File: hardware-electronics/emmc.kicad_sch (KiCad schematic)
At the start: 2 parts, among them U2 EMMC16G-MW28-01E10, U8 USB2244-AEZG-06

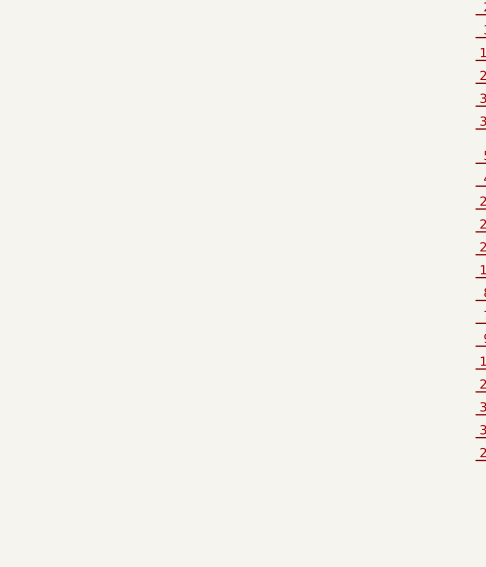
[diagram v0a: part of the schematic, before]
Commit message: SCH organise schematic #7
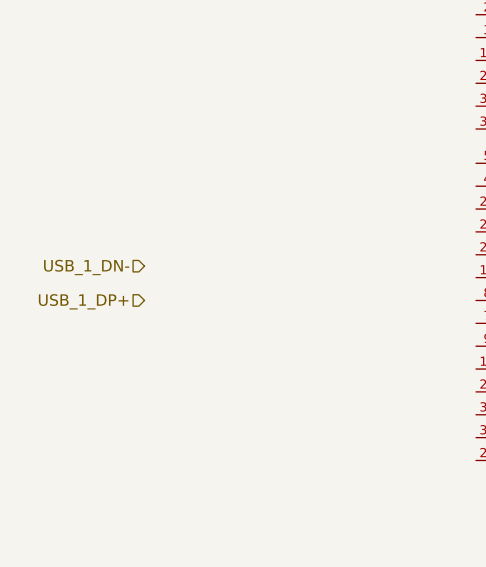
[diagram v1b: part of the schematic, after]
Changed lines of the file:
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@@
 	(generator_version "8.0")
 	(paper "A4")
+	(hierarchical_label "USB_1_DP+"
+		(shape input)
+		(at 58.42 54.61 180)
+		(fields_autoplaced yes)
+		(effects
+			(font
+				(size 1.27 1.27)
+			)
+			(justify right)
+		)
+	)
+	(hierarchical_label "USB_1_DN-"
+		(shape input)
+		(at 58.42 50.8 180)
+		(fields_autoplaced yes)
+		(effects
+			(font
+				(size 1.27 1.27)
+			)
+			(justify right)
+		)
+	)
 	(symbol
 		(lib_id "M2SmartHomeSymbols:USB2244-AEZG-06")

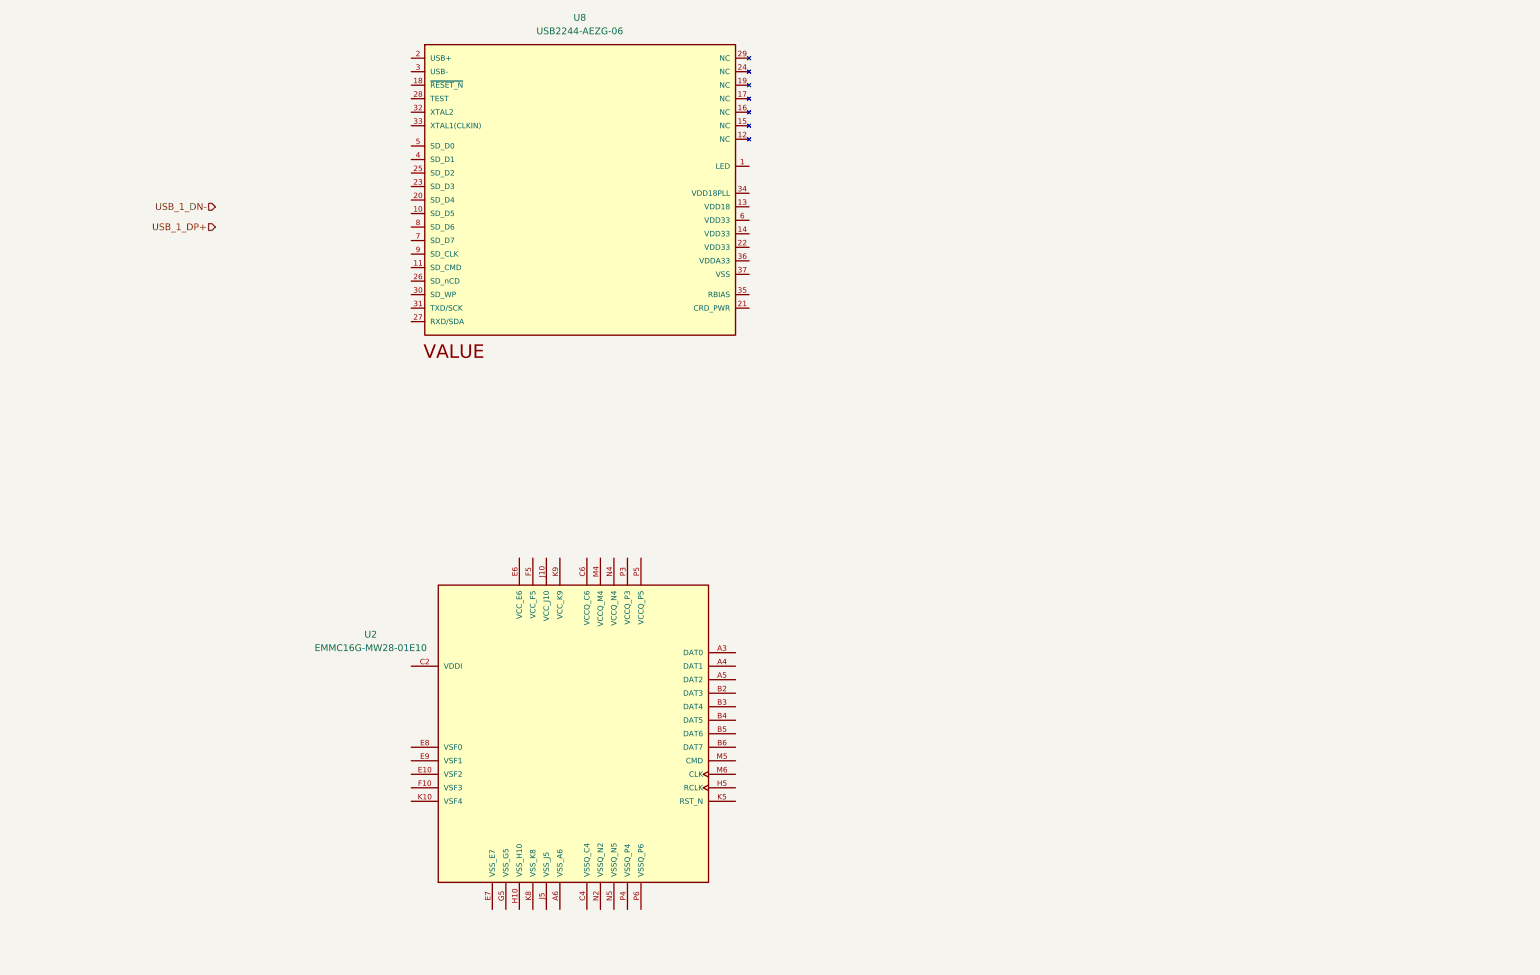
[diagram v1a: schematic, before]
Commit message: WIP SCH EMMC section
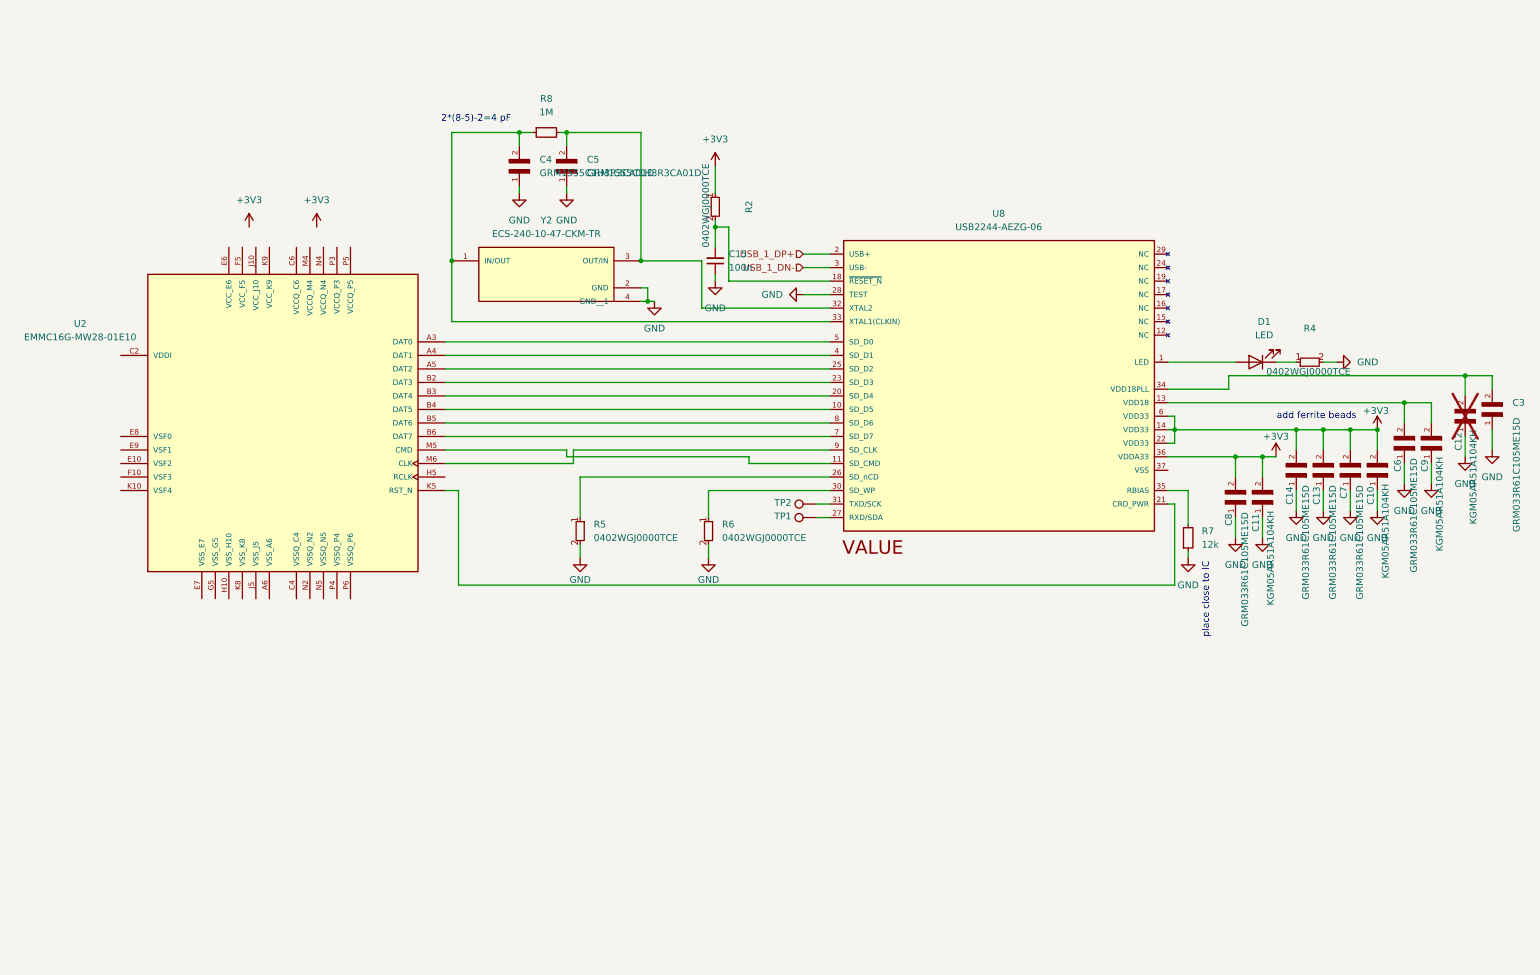
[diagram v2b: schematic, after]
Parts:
- added C10, C11, C12, C9: KGM05AR51A104KH, M2SmartHomeFootprints:KGM05AR51A104KH, symbol M2SmartHomeSymbols:KGM05AR51A104KH
- added C13, C14, C3, C6, C7, C8: GRM033R61C105ME15D, M2SmartHomeFootprints:GRM033R61C105ME15D, symbol M2SmartHomeSymbols:GRM033R61C105ME15D
- added C15: C_100n_0402, C_100n_0402:C_0402_1005Metric, symbol M2SmartHomeSymbols:C_100n_0402
- added C4, C5: GRM1555C1H3R3CA01D, GRM1555C1H3R3CA01D:CAPC1005X55N, symbol M2SmartHomeSymbols:GRM1555C1H3R3CA01D
- added D1: LED, M2SmartHomeFootprints:LED_KPT-1608ZGC, symbol M2SmartHomeSymbols:KP-1608CGCK
- added R2, R4, R5, R6: 0402WGJ0000TCE, M2SmartHomeFootprints:0402WGJ0000TCE, symbol M2SmartHomeSymbols:0402WGJ0000TCE
- added R7: R_12k_0402, R_12k_0402:R_0402_1005Metric, symbol M2SmartHomeSymbols:R_12k_0402
- added R8: R_1M_0402, R_1M_0402:R_0402_1005Metric, symbol M2SmartHomeSymbols:R_1M_0402
- added TP1: TestPoint, TestPoint:TestPoint_Pad_D1.0mm, symbol Connector:TestPoint
- added TP2: TestPoint, symbol Connector:TestPoint
- added Y2: ECS-240-10-47-CKM-TR, M2SmartHomeFootprints:ECS-240-10-47-CKM-TR, symbol M2SmartHomeSymbols:ECS-240-10-47-CKM-TR
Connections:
- net USB_1_DN-: now also U8.3 (USB-)
- net USB_1_DP+: now also U8.2 (USB+)
- net at U8.1 (LED): now also D1.2 (A)
- net at U8.10 (SD_D5): now also U2.B4 (DAT5)
- net at U8.11 (SD_CMD): now also U2.M5 (CMD)
- net at U8.13 (VDD18): now also C6.2, C9.2
- net +3V3: now reaches U8.14 (VDD33)
- net +3V3: now also U8.22 (VDD33), U8.36 (VDDA33), U8.6 (VDD33), C10.2, C11.2, C13.2, C14.2, C7.2, C8.2, R2.1
- net at U8.18 (~{RESET_N}): now also C15.2, R2.2
- net at U8.20 (SD_D4): now also U2.B3 (DAT4)
- net at U8.21 (CRD_PWR): now also U2.K5 (RST_N)
- net at U8.23 (SD_D3): now also U2.B2 (DAT3)
- net at U8.25 (SD_D2): now also U2.A5 (DAT2)
- net at U8.26 (SD_nCD): now also R5.1
- net at U8.27 (RXD/SDA): now also TP1.1
- net GND: now reaches U8.28 (TEST)
- net GND: now also C10.1, C11.1, C12.1, C13.1, C14.1, C15.1, C3.1, C4.1, C5.1, C6.1, C7.1, C8.1, C9.1, R4.2, R5.2, R6.2, R7.1, Y2.2 (GND), Y2.4 (GND__1)
- net at U8.30 (SD_WP): now also R6.1
- net at U8.31 (TXD/SCK): now also TP2.1
- net at U8.32 (XTAL2): now also C5.2, R8.2, Y2.3 (OUT/IN)
- net at U8.33 (XTAL1(CLKIN)): now also C4.2, R8.1, Y2.1 (IN/OUT)
- net at U8.34 (VDD18PLL): now also C12.2, C3.2
- net at U8.35 (RBIAS): now also R7.2
- net at U8.4 (SD_D1): now also U2.A4 (DAT1)
- net at U8.5 (SD_D0): now also U2.A3 (DAT0)
- net at U8.7 (SD_D7): now also U2.B6 (DAT7)
- net at U8.8 (SD_D6): now also U2.B5 (DAT6)
- net at U8.9 (SD_CLK): now also U2.M6 (CLK)
- new net: D1.1 (K), R4.1
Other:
- note added: "2*(8-5)-2=4 pF"
- note added: "add ferrite beads"
- note added: "place close to IC"
- moved on the sheet: U2, U8

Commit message: WIP SCH EMMC clean and components replacements
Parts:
- removed C10, C11, C12, C9: KGM05AR51A104KH, M2SmartHomeFootprints:KGM05AR51A104KH, symbol M2SmartHomeSymbols:KGM05AR51A104KH
- removed C13, C14, C3, C6, C7, C8: GRM033R61C105ME15D, M2SmartHomeFootprints:GRM033R61C105ME15D, symbol M2SmartHomeSymbols:GRM033R61C105ME15D
- removed R2, R4, R5, R6: 0402WGJ0000TCE, M2SmartHomeFootprints:0402WGJ0000TCE, symbol M2SmartHomeSymbols:0402WGJ0000TCE
- added C11, C14, C17, C7, C9: C_1uF_0402, C_1uF_0402:C_0402_1005Metric, symbol M2SmartHomeSymbols:C_1uF_0402
- added C13, C16, C3, C6, C8: C_100n_0402, C_100n_0402:C_0402_1005Metric, symbol M2SmartHomeSymbols:C_100n_0402
- added FB1, FB2: FB_120R_0603, FB_120R_0603:FB_0603_1608Metric, symbol M2SmartHomeSymbols:FB_120R_0603
- added R10, R2, R4, R9: R_0_0402, R_0_0402:R_0402_1005Metric, symbol M2SmartHomeSymbols:R_0_0402
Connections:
- net +3V3: now also FB1.2, FB2.2, R2.2; no longer U8.14 (VDD33), U8.22 (VDD33), U8.36 (VDDA33), U8.6 (VDD33)
- net GND: now also U8.37 (VSS), C11.1, C13.1, C14.1, C16.1, C17.1, C3.1, C6.1, C7.1, C8.1, C9.1, R10.1, R4.1, R9.1
- net XTAL2: now reaches C4.2, R8.1, Y2.1 (IN/OUT)
- net XTAL2: now also U8.32 (XTAL2); no longer U8.33 (XTAL1(CLKIN))
- net XTAL1: now reaches C5.2, R8.2, Y2.3 (OUT/IN)
- net XTAL1: now also U8.33 (XTAL1(CLKIN)); no longer U8.32 (XTAL2)
- net at U8.13 (VDD18): now also C6.2, C7.2
- net ~{reset}: now reaches C15.2, U8.18 (~{RESET_N})
- net ~{reset}: now also R2.1
- net at U8.26 (SD_nCD): now also R10.2
- net at U8.30 (SD_WP): now also R4.2
- net at U8.34 (VDD18PLL): now also C3.2, C9.2
- net at D1.1 (K): now also R9.2
- new net: C11.2, C13.2, C14.2, C8.2, FB1.1, U8.14 (VDD33), U8.22 (VDD33), U8.6 (VDD33)
- new net: C16.2, C17.2, FB2.1, U8.36 (VDDA33)
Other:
- note added: "TBD (no info in docu)"
- moved on the sheet: C15, C4, C5, D1, R7, R8, TP1, TP2, U2, Y2

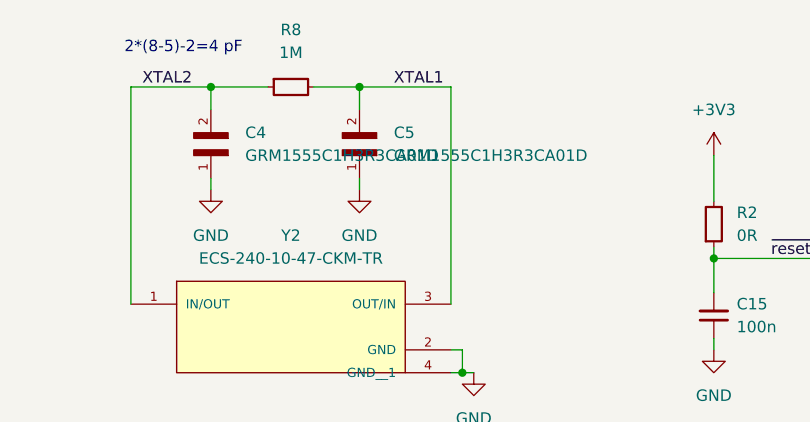
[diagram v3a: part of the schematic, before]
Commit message: WIP SCH EMMC replace OSC capacitors
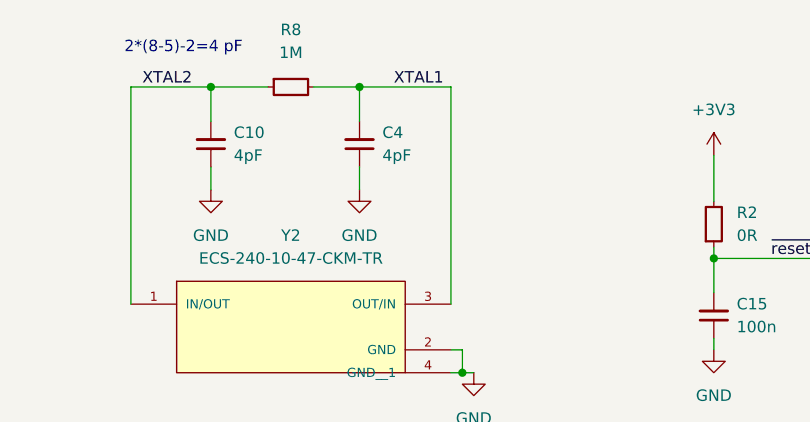
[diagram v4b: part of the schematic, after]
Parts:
- removed C4, C5: GRM1555C1H3R3CA01D, GRM1555C1H3R3CA01D:CAPC1005X55N, symbol M2SmartHomeSymbols:GRM1555C1H3R3CA01D
- added C10, C4: C_4pF_0402, C_4pF_0402:C_0402_1005Metric, symbol M2SmartHomeSymbols:C_4pF_0402
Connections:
- net GND: now also C10.1, C4.1
- net XTAL1: now also C4.2
- net XTAL2: now also C10.2

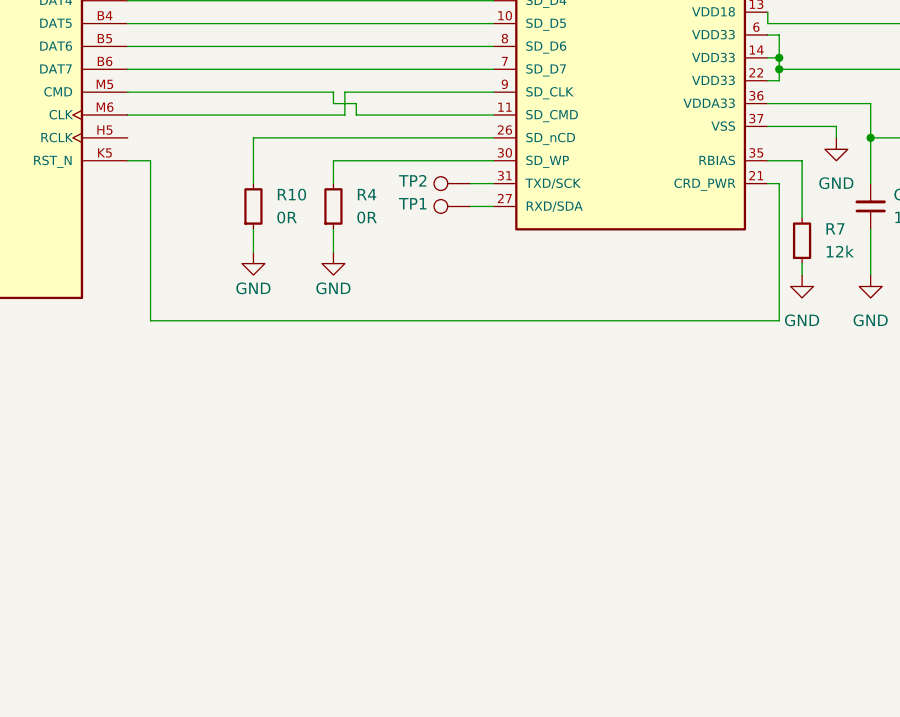
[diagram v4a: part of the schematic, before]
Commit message: WIP SCH EMMC add EEPROM for storing config
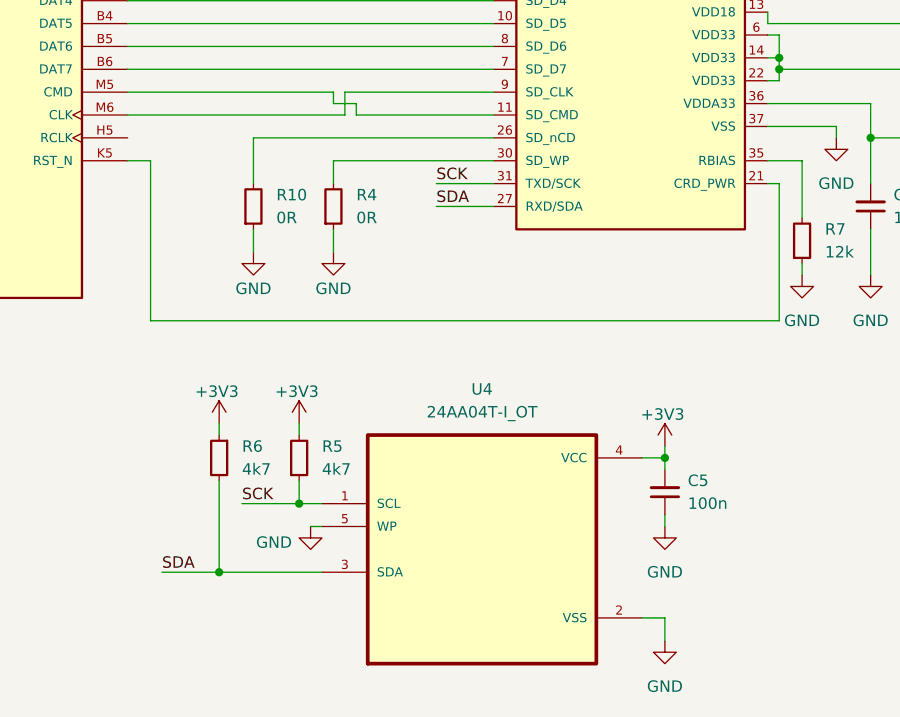
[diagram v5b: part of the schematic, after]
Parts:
- removed TP1: TestPoint, TestPoint:TestPoint_Pad_D1.0mm, symbol Connector:TestPoint
- removed TP2: TestPoint, symbol Connector:TestPoint
- added C5: C_100n_0402, C_100n_0402:C_0402_1005Metric, symbol M2SmartHomeSymbols:C_100n_0402
- added R5, R6: R_4k7_0402, R_4k7_0402:R_0402_1005Metric, symbol M2SmartHomeSymbols:R_4k7_0402
- added U4: 24AA04T-I_OT, M2SmartHomeFootprints:24AA04T-I_OT, symbol M2SmartHomeSymbols:24AA04T-I_OT
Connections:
- net +3V3: now also C5.2, R5.2, R6.1, U4.4 (VCC)
- net GND: now also C5.1, U4.2 (VSS), U4.5 (WP)
- net SDA: now reaches U8.27 (RXD/SDA)
- net SDA: now also R6.2, U4.3 (SDA)
- net SCK: now reaches U8.31 (TXD/SCK)
- net SCK: now also R5.1, U4.1 (SCL)

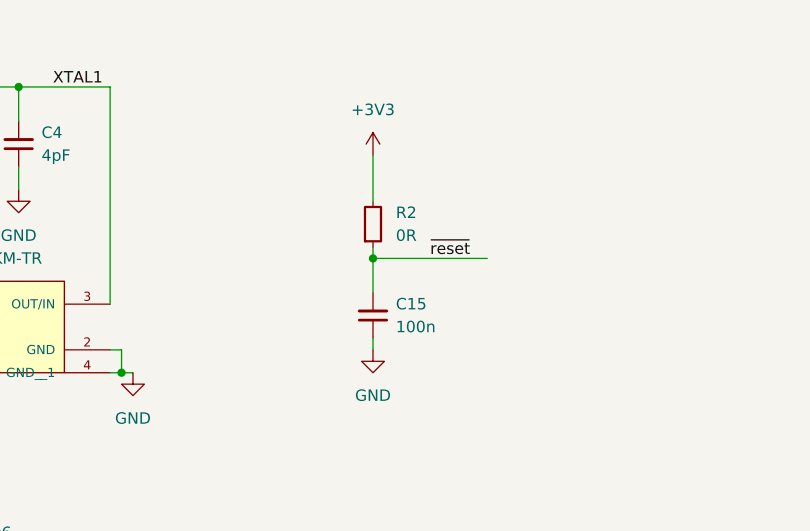
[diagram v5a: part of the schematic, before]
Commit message: WIP SCH EMMC modified reset circuitry
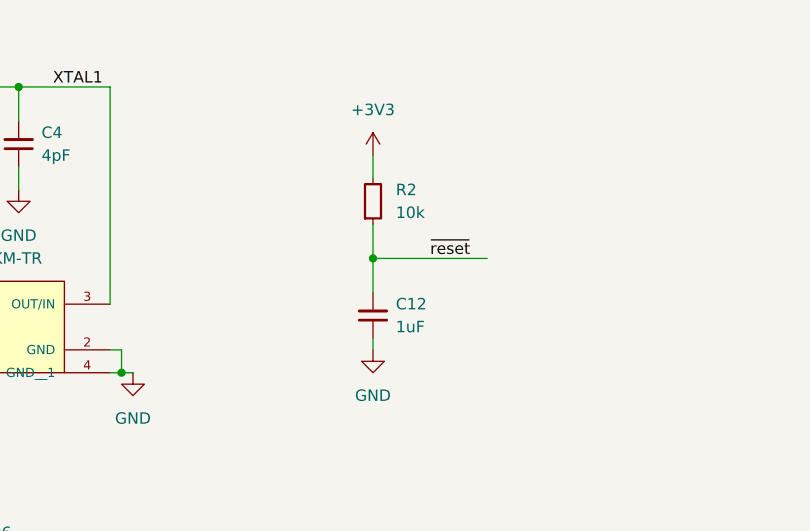
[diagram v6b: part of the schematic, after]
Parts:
- removed C15: C_100n_0402, C_100n_0402:C_0402_1005Metric, symbol M2SmartHomeSymbols:C_100n_0402
- removed R2: R_0_0402, R_0_0402:R_0402_1005Metric, symbol M2SmartHomeSymbols:R_0_0402
- added C12: C_1uF_0402, C_1uF_0402:C_0402_1005Metric, symbol M2SmartHomeSymbols:C_1uF_0402
- added R2: R_10k_0402, R_10k_0402:R_0402_1005Metric, symbol M2SmartHomeSymbols:R_10k_0402
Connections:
- net +3V3: now also R2.2
- net GND: now also C12.1
- net ~{reset}: now also C12.2, R2.1
